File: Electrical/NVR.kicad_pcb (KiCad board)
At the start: 4 copper layers, 120 x 120 mm, 400 parts, among them IC1 RTL8125BG-CG, IC2 SiC437AED-T1-GE3, IC4 RTL8125BG-CG, J1 Bus_M.2_Socket_M, J10 87427-0442, J11 SS-60300-011, J12 Conn_01x03_Pin, J13 SATA-A-PL-SMT-K, J14 SATA-A-PL-SMT-K, J15 Conn_01x03_Pin, J16 USB_C_Receptacle_USB2.0, J17 53261-0271, J19 SATA-A-PL-SMT-K, J2 SS-60300-011, J20 SATA-A-PL-SMT-K, J21 SATA-A-PL-SMT-K, J22 SATA-A-PL-SMT-K, J3 HDMI_A, J4 USB3_A_Stacked, J5 USB_A_Stacked, J6 Bus_M.2_Socket_E, J7 87427-0442, J8 87427-0442, J9 87427-0442, M1 Fan_4pin, M2 Fan_4pin, Q1 2N7002, Q10 2N7002, Q2 2SK3018, Q3 2SK3018, Q4 2SK3018, Q8 2N7002, Q9 2N7002, SW1 SW_Push, U1 TPAZ1023-04F, U11 W25Q128JVSIQ, U13 HT7533, U14 CH224Q_C46061833, U15 SY8253ADC, U16 SY8253ADC, U2 TPAZ1023-04F, U3 ULC0524P, U4 ULC0524P, U5 ULC0524P, U6 SY8253ADC, U7 SY8253ADC, U79 W25Q128JVSIQ, U8 ASM1166, Y1 25MHz, Y2 25MHz, Y4 25MHz

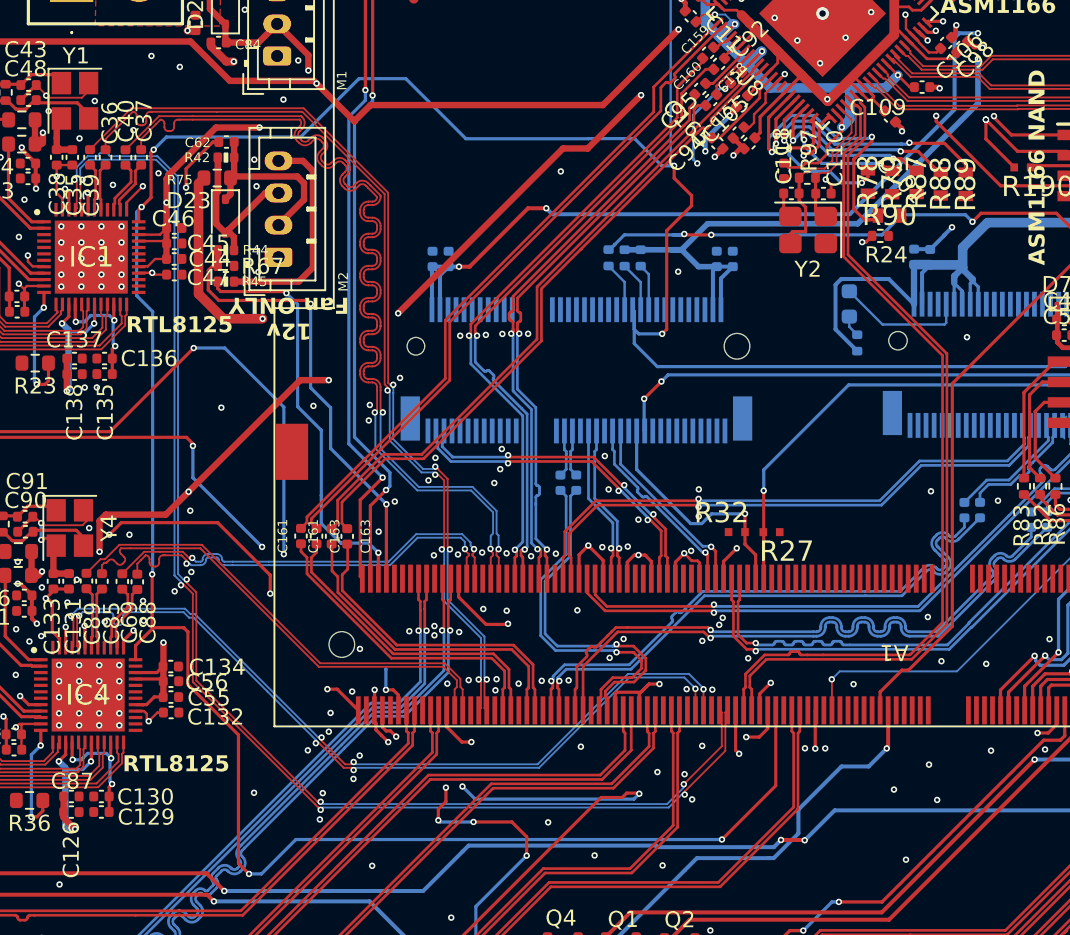
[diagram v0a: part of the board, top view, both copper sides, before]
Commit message: Fix Ground Plane Intteruptions
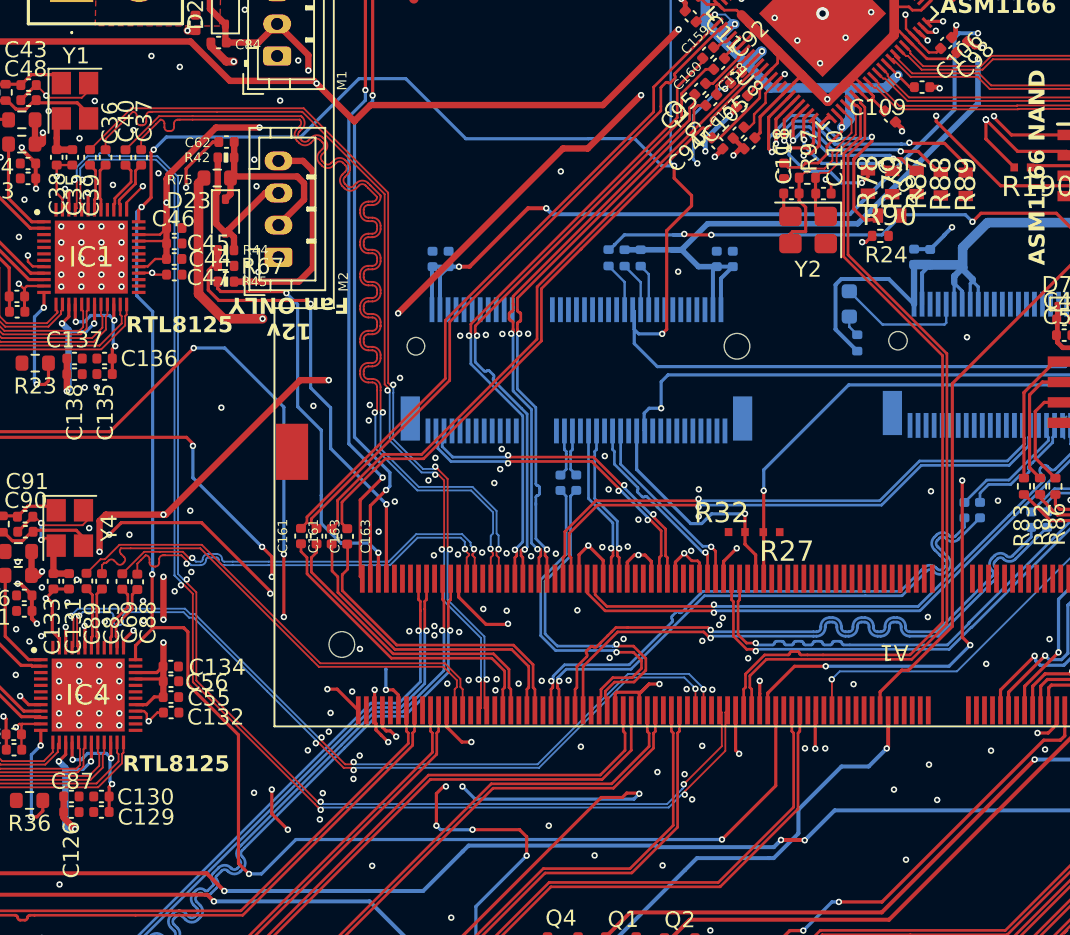
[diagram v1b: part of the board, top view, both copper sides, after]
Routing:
- net /~{WAKE}: track 61.6 -> 86.9 mm, vias 3 -> 4
- net +0V9: track 206.8 -> 193.8 mm
- net /LattePanda Module/SLS_S3: track 41.3 -> 49.6 mm
- net /~{PWR_LED}/~{PSON}: track 175.0 -> 180.6 mm, vias 10 -> 11
- net +BATT: track 118.9 -> 122.5 mm, vias 7 -> 9
- net +5V: track 95.4 -> 93.1 mm
- net +3V3: track 943.2 -> 941.2 mm, vias 76 -> 78
- net GND: track 255.3 -> 255.1 mm, vias 408 -> 407
- net /LattePanda Module/~{PWR_SW}: vias 5 -> 6
